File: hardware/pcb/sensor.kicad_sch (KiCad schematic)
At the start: 0 parts

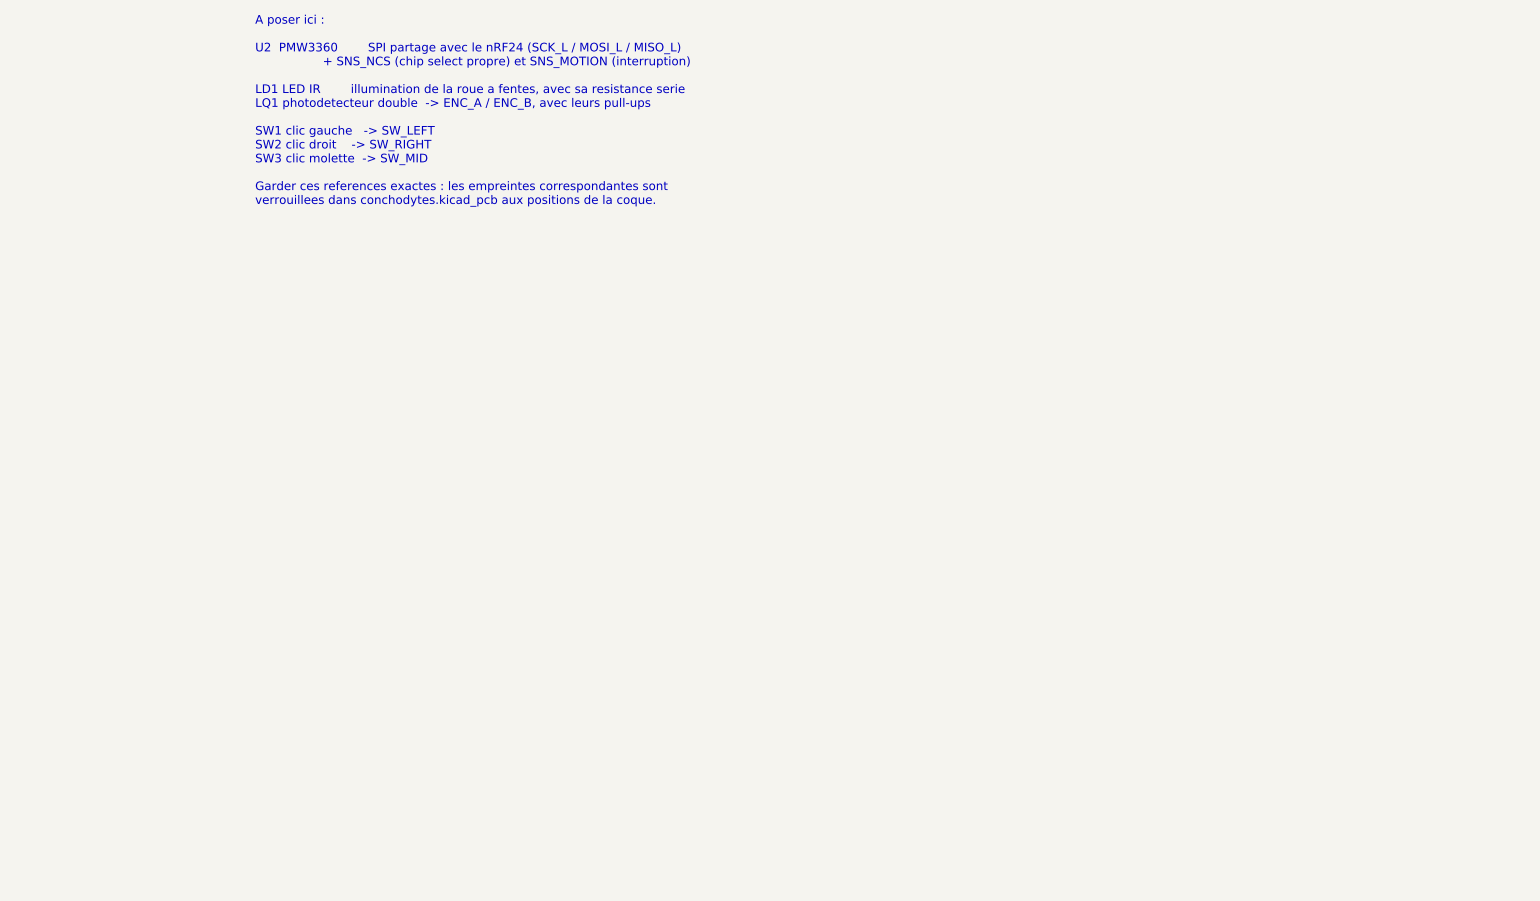
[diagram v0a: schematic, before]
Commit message: schéma du capteur, de l'encodeur et des clics
sensor.kicad_sch, généré et vérifié par netlist :

- U2 PMW3360 — SPI partagé avec le nRF24 (SCK_L/MOSI_L/MISO_L, déjà routés vers
  le S3 par leurs 100 ohms), plus SNS_NCS et SNS_MOTION en propre. NRESET tiré
  au 3,3 V, LED_P pilote D100 via R101.
- U100 LDO 1,8 V dédié : VDD et VDDPIX du capteur ne sont PAS en 3,3 V (plage
  usuelle 1,8-2,1 V, à confirmer datasheet). VDDIO reste en 3,3 V.
  Découplages C100/C101 (VDD, VDDPIX), C102 (VDDIO), C103 (bulk 1,8 V).
- LD1 + R102 : LED d'illumination de la roue à 60 fentes.
  LQ1 double phototransistor, commun à la masse, voies ENC_A/ENC_B avec leurs
  pull-ups R103/R104.
- SW1/SW2/SW3 : COM à la masse, NO vers SW_LEFT/SW_RIGHT/SW_MID avec pull-ups.

Les 6 références imposées par la coque sont respectées — SW1/SW2/SW3, LD1, LQ1,
U2 — pour que le F8 retrouve les empreintes verrouillées du PCB.

Côté MCU, les 7 signaux sont accrochés sur des GPIO libérés par le clavier, en
évitant les broches de strapping et la PSRAM octale :
  GPIO4 SNS_NCS · GPIO5 SNS_MOTION · GPIO7 ENC_A · GPIO17 ENC_B
  GPIO18 SW_LEFT · GPIO19 SW_RIGHT · GPIO20 SW_MID

Deux pièges rencontrés en écrivant ces feuilles, tous deux attrapés par la
netlist : placer des fils à des coordonnées devinées ne connecte rien (il faut
calculer la position réelle des pins depuis lib_symbols), et insérer sur la
première occurrence de (embedded_fonts tombe à l'intérieur des définitions de
symboles et casse le fichier.

Co-Authored-By: Claude Opus 5 <noreply@anthropic.com>
Claude-Session: https://claude.ai/code/session_01GfX5RmekmQi78Dm37qsT4Z
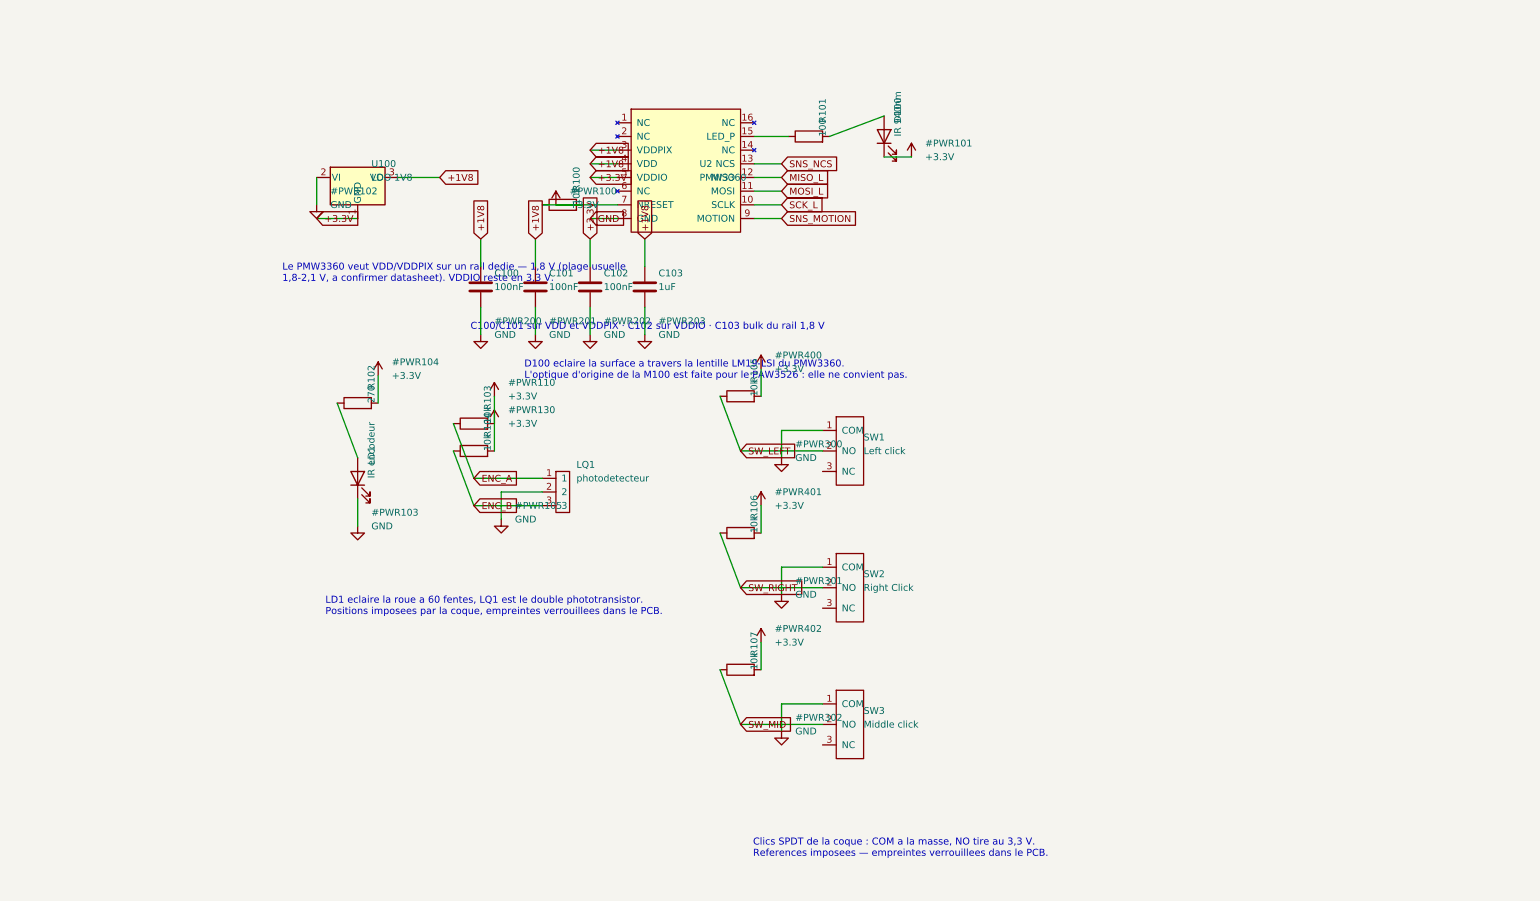
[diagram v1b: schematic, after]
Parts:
- added C100, C101, C102: 100nF, Capacitor_SMD:C_0603_1608Metric, symbol Device:C
- added C103: 1uF, Capacitor_SMD:C_0603_1608Metric, symbol Device:C
- added D100: IR 940nm, LED_SMD:LED_0805_2012Metric, symbol Device:LED
- added LD1: IR encodeur, Mouse:Rot_LED, symbol Device:LED
- added LQ1: photodetecteur, Mouse:LQ1, symbol Optical_Mouse:LQ
- added R100, R103, R104, R105, R106, R107: 10k, Resistor_SMD:R_0603_1608Metric, symbol Device:R
- added R101: 100, Resistor_SMD:R_0603_1608Metric, symbol Device:R
- added R102: 270, Resistor_SMD:R_0603_1608Metric, symbol Device:R
- added SW1: Left click, Mouse:SPDT_Switch, symbol Optical_Mouse:switch
- added SW2: Right Click, Mouse:SPDT_Switch, symbol Optical_Mouse:switch
- added SW3: Middle click, Mouse:SPDT_Switch, symbol Optical_Mouse:switch
- added U100: LDO 1V8, Package_TO_SOT_SMD:SOT-23, symbol Regulator_Linear:MCP1700x-330xxTT
- added U2: PMW3360, PMW3360:PMW3360, symbol PMW3360:PMW3360
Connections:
- new net: R101.1, U2.15 (LED_P)
- new net: D100.2 (A), R101.2
- new net: LD1.2 (A), R102.1
- new net +1V8: C100.1, C101.1, C103.1, U100.3 (VO), U2.3 (VDDPIX), U2.4 (VDD)
- new net +3.3V: C102.1, D100.1 (K), R100.1, R100.2, R102.2, R103.2, R104.2, R105.2, R106.2, R107.2, U100.1 (GND), U2.5 (VDDIO), U2.7 (NRESET)
- new net ENC_A: LQ1.1, R103.1
- new net ENC_B: LQ1.3, R104.1
- new net GND: C100.2, C101.2, C102.2, C103.2, LD1.1 (K), LQ1.2, SW1.1 (COM), SW2.1 (COM), SW3.1 (COM), U100.2 (VI), U2.8 (GND)
- new net MISO_L: U2.12 (MISO)
- new net MOSI_L: U2.11 (MOSI)
- new net SCK_L: U2.10 (SCLK)
- new net SNS_MOTION: U2.9 (MOTION)
- new net SNS_NCS: U2.13 (NCS)
- new net SW_LEFT: R105.1, SW1.2 (NO)
- new net SW_MID: R107.1, SW3.2 (NO)
- new net SW_RIGHT: R106.1, SW2.2 (NO)
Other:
- note added: "C100/C101 sur VDD et VDDPIX · C102 sur VDDIO · C103 bulk du rail 1,8 V"
- note added: "Clics SPDT de la coque : COM a la masse, NO tire au 3,3 V. References imposees — empreintes verrouillees dans le PCB."
- note added: "D100 eclaire la surface a travers la lentille LM19-LSI du PMW3360. L'optique d'origine de la M100 est faite pour le PAW3526 : elle ne convient pas."
- note added: "LD1 eclaire la roue a 60 fentes, LQ1 est le double phototransistor. Positions imposees par la coque, empreintes verrouillees dans le PCB."
- note added: "Le PMW3360 veut VDD/VDDPIX sur un rail dedie — 1,8 V (plage usuelle 1,8-2,1 V, a confirmer datasheet). VDDIO reste en 3,3 V."
- note removed: "A poser ici : U2 PMW3360 SPI partage avec le nRF24 (SCK_L / MOSI_L / MISO_L) + SNS_NCS (chip select propre) et SNS_MOTION (interruption) LD1 LED IR illumination de la roue a fentes, avec sa resistance serie LQ1 photodetecteur double -> ENC_A / ENC_B, avec leurs pull-ups SW1 clic gauche -> SW_LEFT SW2 clic droit -> SW_RIGHT SW3 clic molette -> SW_MID Garder ces references exactes : les empreintes 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"

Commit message: tout sur la grille de 1,27 + correction du brochage du LDO
Mes origines de placement (100, 60...) n'étaient pas des multiples de 1,27, donc
rien de ce qui en dérivait ne tombait sur la grille : 89 endpoint_off_grid, et
Mae aurait dû tout redéplacer à la main. Les coordonnées sont maintenant snappées
à la source, dans les primitives de placement, de fil et de label. Vérifié :
zéro coordonnée hors grille hors lib_symbols, et les 7 liaisons capteur <-> S3
ont survécu au snap.

Correction électrique : j'avais câblé le LDO du capteur à l'envers — 3,3 V sur
la pin de masse. Le symbole porte encore le lib_id MCP1700 mais son brochage a
été corrigé pour le HT7833 SOT-89 pendant la revue du clavier : 1=GND, 2=VI,
3=VO. C'est exactement le piège qui avait donné le bloquant du Niphargus, et
c'est l'ERC qui l'a rattrapé (ground_pin_not_ground + power_pin_not_driven).

ERC : 125 -> 36 -> 20 violations.

Co-Authored-By: Claude Opus 5 <noreply@anthropic.com>
Claude-Session: https://claude.ai/code/session_01GfX5RmekmQi78Dm37qsT4Z
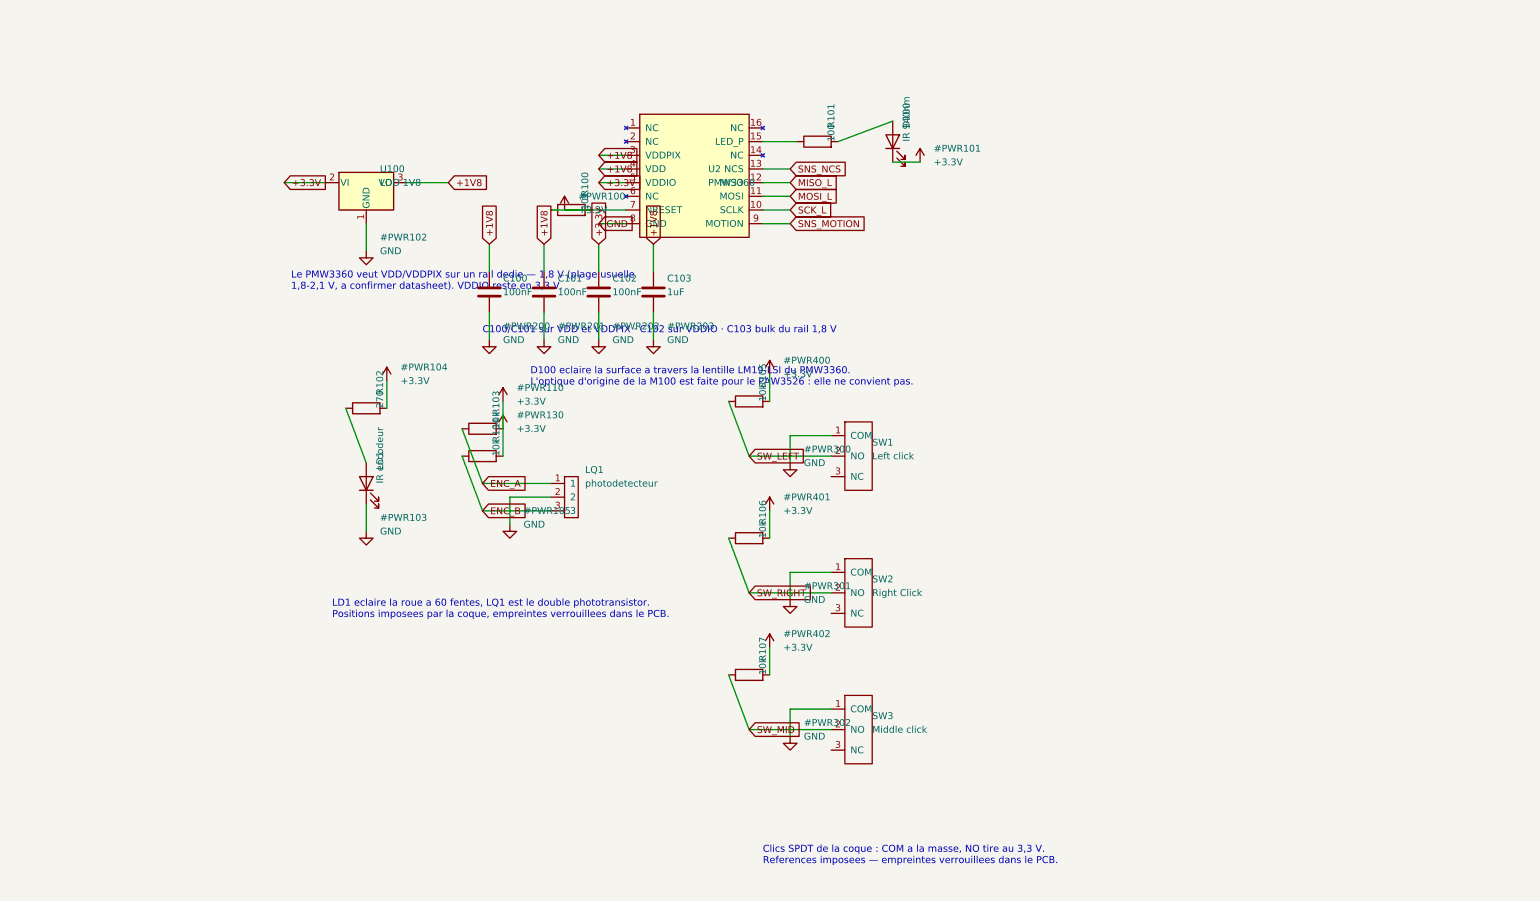
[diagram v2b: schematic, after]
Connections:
- net +3.3V: now also U100.2 (VI); no longer U100.1 (GND)
- net GND: now also U100.1 (GND); no longer U100.2 (VI)

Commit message: lien schéma <-> PCB : les 6 empreintes de la coque sont remariées
Les empreintes verrouillées portaient encore les path UUID du fork
(/00000000-...-62f7695e), donc aucune n'était liée aux symboles du schéma : un
F8 les aurait dissociées ou dupliquées, et les positions imposées par la coque
étaient perdues.

Chaque path pointe maintenant sur l'uuid du symbole correspondant dans
sensor.kicad_sch — SW1/SW2/SW3, LD1, LQ1, U2. Même technique que la
réconciliation des 105 empreintes du Niphargus.

Aussi : 8 no-connect posés sur les broches NC du PMW3360 et des trois SPDT,
en calculant leur position réelle depuis lib_symbols.

Co-Authored-By: Claude Opus 5 <noreply@anthropic.com>
Claude-Session: https://claude.ai/code/session_01GfX5RmekmQi78Dm37qsT4Z
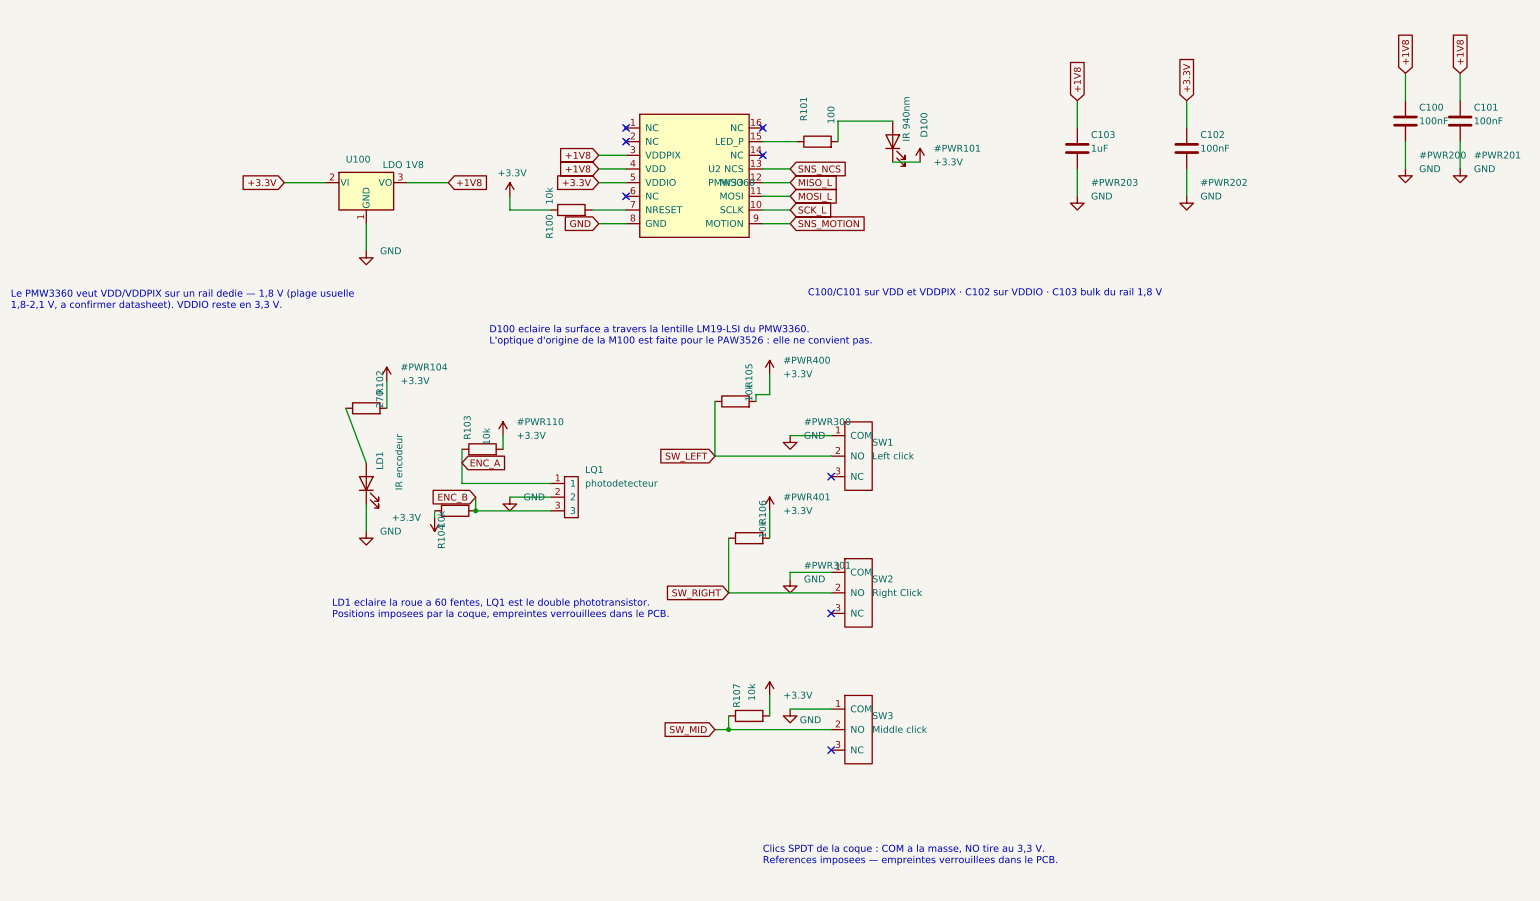
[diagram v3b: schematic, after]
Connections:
- net +3.3V: no longer R100.2, U2.7 (NRESET)
- new net: R100.2, U2.7 (NRESET)
- no-connect marks 0 -> 8
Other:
- moved on the sheet: C100, C101, C102, C103, R103, R104, R105, R107

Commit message: contacts NC des trois clics : anti-rebond par SPDT
Les switches de la coque M100 sont des SPDT. Le schema n'exploitait que COM et
NO, les pins NC portaient un no_connect et leurs pads restaient en l'air.

On lit maintenant les DEUX contacts. Au repos NC est ferme sur COM donc bas et
NO ouvert donc haut ; au clic ils s'inversent. Pendant le rebond les deux sont
hauts : le firmware garde alors l'etat precedent, ce qui supprime le double-clic
sans aucun filtrage temporel.

  SW_LEFT_NC  -> GPIO4    SW_RIGHT_NC -> GPIO5    SW_MID_NC -> GPIO6
  pull-ups 10 k R108/R109/R110, en miroir des R105-R107 des NO

L'ERC y GAGNE 3 erreurs (14 -> 11) : GPIO4/5/6 etaient des pins libres
signalees pin_not_connected. Netlist verifiee, chaque net NC a exactement
3 noeuds. DRC 26/20 inchange, 0 pad non connecte. Placement et routage par Mae.

CORRECTION DE DOCUMENTATION : le README donnait "SW_LEFT 18, SW_RIGHT 19,
SW_MID 20" — ce sont les NUMEROS DE BROCHE du module, pas les GPIO, qui valent
10/11/12. Idem SNS_NCS (GPIO17, broche 10) et SNS_MOTION (GPIO18, broche 11).
Verifie en recoupant lib_symbols, les fils et la netlist. Le tableau donne
desormais les deux colonnes. Le module au BOM est un N8R2 (C2913204), pas le
N16R8 dont parlait le README — la mention de PSRAM octale est retiree.

Co-Authored-By: Claude Opus 5 <noreply@anthropic.com>
Claude-Session: https://claude.ai/code/session_01GfX5RmekmQi78Dm37qsT4Z
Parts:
- added R108, R109, R110: 10k, Resistor_SMD:R_0603_1608Metric, symbol Device:R
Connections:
- net +3.3V: now also R108.2, R109.2, R110.2
- net SW_MID_NC: now reaches SW3.3 (NC)
- net SW_MID_NC: now also R110.1
- net SW_LEFT_NC: now reaches SW1.3 (NC)
- net SW_LEFT_NC: now also R108.1
- net SW_RIGHT_NC: now reaches SW2.3 (NC)
- net SW_RIGHT_NC: now also R109.1
- no-connect marks 8 -> 5
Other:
- note added: "Clics SPDT de la coque : COM a la masse, NO et NC tires chacun au 3,3 V. Lire les deux contacts en parallele = anti-rebond : pendant le rebond les deux sont hauts, le firmware garde l'etat precedent au lieu de compter un faux clic. References imposees — empreintes verrouillees dans le PCB."
- note removed: "Clics SPDT de la coque : COM a la masse, NO tire au 3,3 V. References imposees — empreintes verrouillees dans le PCB."
